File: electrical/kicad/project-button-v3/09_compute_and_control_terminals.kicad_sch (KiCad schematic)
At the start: 3 parts

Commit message: Add native DYNAMIXEL star injection release candidate
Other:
- title: PB HR-V0 Electrical V3 - 09 -> PB HR-V0 V3-P1.2 - 09
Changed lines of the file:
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@@
   (version 20250114) (generator "eeschema") (generator_version "10.0")
  (paper "A3")
-  (title_block (title "PB HR-V0 Electrical V3 - 09") (date "2026-08-06") (rev "V3-P1.1")
+  (title_block (title "PB HR-V0 V3-P1.2 - 09") (date "2026-08-07") (rev "V3-P1.2")
     (company "Project Button") (comment 1 "PRELIMINARY - NOT APPROVED FOR FABRICATION OR ENERGIZATION") (comment 2 "CONNECTED DESIGN CANDIDATE - QUALIFIED REVIEW REQUIRED"))
   (text "PRELIMINARY - NOT APPROVED FOR FABRICATION OR ENERGIZATION" (exclude_from_sim no) (at 17.78 10.16 0)

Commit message: Document HR-V0 contactor application evidence
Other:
- title: PB HR-V0 V3-P1.2 - 09 -> PB HR-V0 V3-P1.3 - 09
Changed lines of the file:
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@@
   (version 20250114) (generator "eeschema") (generator_version "10.0")
  (paper "A3")
-  (title_block (title "PB HR-V0 V3-P1.2 - 09") (date "2026-08-07") (rev "V3-P1.2")
+  (title_block (title "PB HR-V0 V3-P1.3 - 09") (date "2026-08-07") (rev "V3-P1.3")
     (company "Project Button") (comment 1 "PRELIMINARY - NOT APPROVED FOR FABRICATION OR ENERGIZATION") (comment 2 "CONNECTED DESIGN CANDIDATE - QUALIFIED REVIEW REQUIRED"))
   (text "PRELIMINARY - NOT APPROVED FOR FABRICATION OR ENERGIZATION" (exclude_from_sim no) (at 17.78 10.16 0)

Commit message: Add received-lot control for reset and arm terminals
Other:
- title: PB HR-V0 V3-P1.3 - 09 -> PB HR-V0 V3-P1.4 - 09
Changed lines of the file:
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@@
   (version 20250114) (generator "eeschema") (generator_version "10.0")
  (paper "A3")
-  (title_block (title "PB HR-V0 V3-P1.3 - 09") (date "2026-08-07") (rev "V3-P1.3")
+  (title_block (title "PB HR-V0 V3-P1.4 - 09") (date "2026-08-07") (rev "V3-P1.4")
     (company "Project Button") (comment 1 "PRELIMINARY - NOT APPROVED FOR FABRICATION OR ENERGIZATION") (comment 2 "CONNECTED DESIGN CANDIDATE - QUALIFIED REVIEW REQUIRED"))
   (text "PRELIMINARY - NOT APPROVED FOR FABRICATION OR ENERGIZATION" (exclude_from_sim no) (at 17.78 10.16 0)

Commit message: Reconcile H1 pilot light in electrical V3
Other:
- title: PB HR-V0 V3-P1.4 - 09 -> PB HR-V0 V3-P1.5 - 09
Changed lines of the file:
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@@
   (version 20250114) (generator "eeschema") (generator_version "10.0")
  (paper "A3")
-  (title_block (title "PB HR-V0 V3-P1.4 - 09") (date "2026-08-07") (rev "V3-P1.4")
+  (title_block (title "PB HR-V0 V3-P1.5 - 09") (date "2026-08-07") (rev "V3-P1.5")
     (company "Project Button") (comment 1 "PRELIMINARY - NOT APPROVED FOR FABRICATION OR ENERGIZATION") (comment 2 "CONNECTED DESIGN CANDIDATE - QUALIFIED REVIEW REQUIRED"))
   (text "PRELIMINARY - NOT APPROVED FOR FABRICATION OR ENERGIZATION" (exclude_from_sim no) (at 17.78 10.16 0)

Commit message: Correct control-panel protection fit
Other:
- title: PB HR-V0 V3-P1.5 - 09 -> PB HR-V0 V3-P1.6 - 09
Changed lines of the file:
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@@
   (version 20250114) (generator "eeschema") (generator_version "10.0")
  (paper "A3")
-  (title_block (title "PB HR-V0 V3-P1.5 - 09") (date "2026-08-07") (rev "V3-P1.5")
+  (title_block (title "PB HR-V0 V3-P1.6 - 09") (date "2026-08-07") (rev "V3-P1.6")
     (company "Project Button") (comment 1 "PRELIMINARY - NOT APPROVED FOR FABRICATION OR ENERGIZATION") (comment 2 "CONNECTED DESIGN CANDIDATE - QUALIFIED REVIEW REQUIRED"))
   (text "PRELIMINARY - NOT APPROVED FOR FABRICATION OR ENERGIZATION" (exclude_from_sim no) (at 17.78 10.16 0)

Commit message: Screen service disconnect and freeze fuse end cover
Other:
- title: PB HR-V0 V3-P1.6 - 09 -> PB HR-V0 V3-P1.7 - 09
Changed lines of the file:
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@@
   (version 20250114) (generator "eeschema") (generator_version "10.0")
  (paper "A3")
-  (title_block (title "PB HR-V0 V3-P1.6 - 09") (date "2026-08-07") (rev "V3-P1.6")
+  (title_block (title "PB HR-V0 V3-P1.7 - 09") (date "2026-08-07") (rev "V3-P1.7")
     (company "Project Button") (comment 1 "PRELIMINARY - NOT APPROVED FOR FABRICATION OR ENERGIZATION") (comment 2 "CONNECTED DESIGN CANDIDATE - QUALIFIED REVIEW REQUIRED"))
   (text "PRELIMINARY - NOT APPROVED FOR FABRICATION OR ENERGIZATION" (exclude_from_sim no) (at 17.78 10.16 0)

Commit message: Freeze SD1 candidate and synchronize R64
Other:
- title: PB HR-V0 V3-P1.7 - 09 -> PB HR-V0 V3-P1.8 - 09
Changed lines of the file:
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@@
   (version 20250114) (generator "eeschema") (generator_version "10.0")
  (paper "A3")
-  (title_block (title "PB HR-V0 V3-P1.7 - 09") (date "2026-08-07") (rev "V3-P1.7")
+  (title_block (title "PB HR-V0 V3-P1.8 - 09") (date "2026-08-07") (rev "V3-P1.8")
     (company "Project Button") (comment 1 "PRELIMINARY - NOT APPROVED FOR FABRICATION OR ENERGIZATION") (comment 2 "CONNECTED DESIGN CANDIDATE - QUALIFIED REVIEW REQUIRED"))
   (text "PRELIMINARY - NOT APPROVED FOR FABRICATION OR ENERGIZATION" (exclude_from_sim no) (at 17.78 10.16 0)

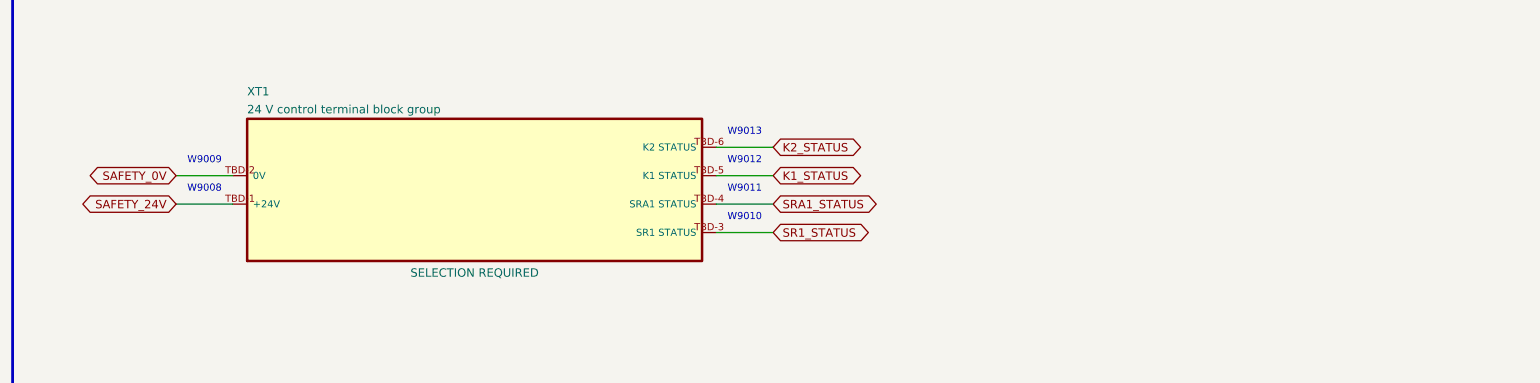
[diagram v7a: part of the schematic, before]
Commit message: Add R79 E2 hardware slice and Electrical V3-P1.9
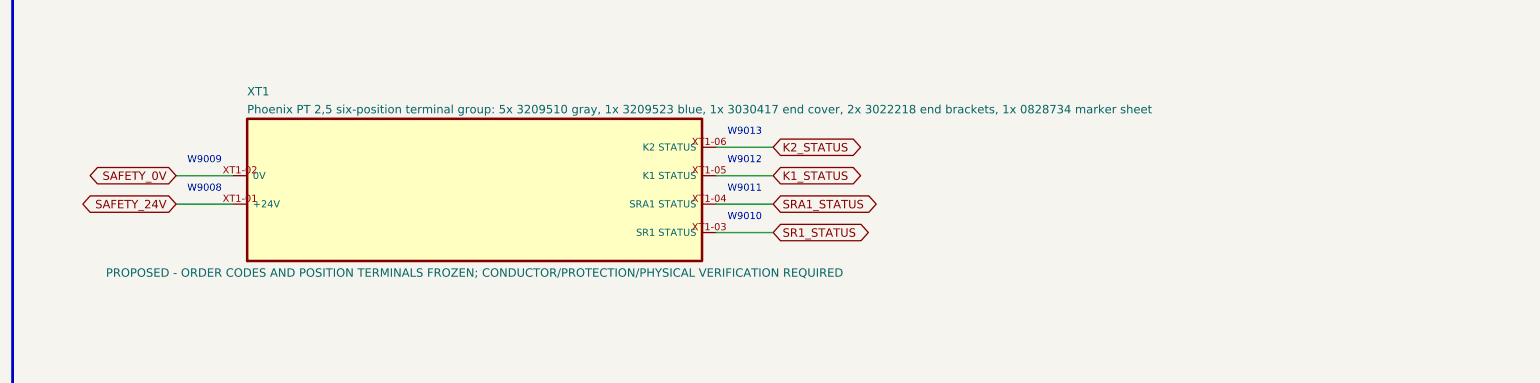
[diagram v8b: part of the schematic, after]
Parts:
- XT1: value 24 V control terminal block group -> Phoenix PT 2,5 six-position terminal group: 5x 3209510 gray, 1x 3209523 blue, 1x 3030417 end cover, 2x 3022218 end brac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; Display 24 V control terminal block group -> Phoenix PT 2,5 six-position terminal group: 5x 3209510 gray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; Evidence (none) -> Phoenix Contact current official product records for items 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; Status SELECTION REQUIRED -> PROPOSED - ORDER CODES AND POSITION TERMINALS FROZEN; CONDU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
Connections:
- net K1_STATUS: now also XT1.XT1-05 (K1 STATUS); no longer XT1.TBD-5 (K1 STATUS)
- net K2_STATUS: now also XT1.XT1-06 (K2 STATUS); no longer XT1.TBD-6 (K2 STATUS)
- net SAFETY_0V: now also XT1.XT1-02 (0V); no longer XT1.TBD-2 (0V)
- net SAFETY_24V: now also XT1.XT1-01 (+24V); no longer XT1.TBD-1 (+24V)
- net SR1_STATUS: now also XT1.XT1-03 (SR1 STATUS); no longer XT1.TBD-3 (SR1 STATUS)
- net SRA1_STATUS: now also XT1.XT1-04 (SRA1 STATUS); no longer XT1.TBD-4 (SRA1 STATUS)
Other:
- title: PB HR-V0 V3-P1.8 - 09 -> PB HR-V0 V3-P1.9 - 09
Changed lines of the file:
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@@
   (version 20250114) (generator "eeschema") (generator_version "10.0")
  (paper "A3")
-  (title_block (title "PB HR-V0 V3-P1.8 - 09") (date "2026-08-07") (rev "V3-P1.8")
+  (title_block (title "PB HR-V0 V3-P1.9 - 09") (date "2026-08-08") (rev "V3-P1.9")
     (company "Project Button") (comment 1 "PRELIMINARY - NOT APPROVED FOR FABRICATION OR ENERGIZATION") (comment 2 "CONNECTED DESIGN CANDIDATE - QUALIFIED REVIEW REQUIRED"))
   (text "PRELIMINARY - NOT APPROVED FOR FABRICATION OR ENERGIZATION" (exclude_from_sim no) (at 17.78 10.16 0)
@@
       (exclude_from_sim no) (in_bom yes) (on_board yes) (dnp no)
       (property "Reference" "XT1" (at 54.61 182.69 0) (effects (font (size 1.50 1.50)) (justify left bottom)))
-      (property "Value" "24 V control terminal block group" (at 95.25 199.39 0) (effects (font (size 1.50 1.50)) (hide yes)))
+      (property "Value" "Phoenix PT 2,5 six-position terminal group: 5x 3209510 gray, 1x 3209523 blue, 1x 3030417 end cover, 2x 3022218 end brackets, 1x 0828734 marker sheet" (at 95.25 199.39 0) (effects (font (size 1.50 1.50)) (hide yes)))
       (property "Footprint" "" (at 95.25 199.39 0) (effects (font (size 1.50 1.50)) (hide yes)))
-      (property "Datasheet" "" (at 95.25 199.39 0) (effects (font (size 1.50 1.50)) (hide yes)))
-      (property "Description" "Exact terminal family, end covers, jumpers, markers, conductor range and torque open." (at 95.25 199.39 0) (effects (font (size 1.50 1.50)) (hide yes)))
-      (property "Status" "SELECTION REQUIRED" (at 95.25 215.09 0) (effects (font (size 1.50 1.50)) (justify bottom)))
-      (property "Evidence" "" (at 95.25 199.39 0) (effects (font (size 1.50 1.50)) (hide yes)))
-      (property "Display" "24 V control terminal block group" (at 54.61 185.89 0) (effects (font (size 1.50 1.50)) (justify left bottom)))
-      (pin "TBD-1")
-      (pin "TBD-2")
-      (pin "TBD-3")
-      (pin "TBD-4")
-      (pin "TBD-5")
-      (pin "TBD-6")
+      (property "Datasheet" "https://www.phoenixcontact.com/en-us/products/feed-through-terminal-block-pt-25-3209510" (at 95.25 199.39 0) (effects (font (size 1.50 1.50)) (hide yes)))
+      (property "Description" "Exact six-position family and position-to-net allocation are frozen with no bridges. PT 2,5 item 3209510 and blue item 3209523 each provide two push-in connections and 5.2 mm width; D-ST 2,5 item 3030417 is the open-side end cover; two CLIPFIX 35 item 3022218 end brackets retain the group; UCT-TM 5 item 0828734 supplies 5.2 mm markers. Conductor order code, ferrule/direct-wire method, protection, current/temperature coordination, received compatibility, strip length, installed retention, marking and point-to-point evidence remain open." (at 95.25 199.39 0) (effects (font (size 1.50 1.50)) (hide yes)))
+      (property "Status" "PROPOSED - ORDER CODES AND POSITION TERMINALS FROZEN; CONDUCTOR/PROTECTION/PHYSICAL VERIFICATION REQUIRED" (at 95.25 215.09 0) (effects (font (size 1.50 1.50)) (justify bottom)))
+      (property "Evidence" "Phoenix Contact current official product records for items 3209510, 3209523, 3030417, 3022218 and 0828734; rechecked 2026-08-08." (at 95.25 199.39 0) (effects (font (size 1.50 1.50)) (hide yes)))
+      (property "Display" "Phoenix PT 2,5 six-position terminal group: 5x 3209510 gray, 1x 3209523 blue, 1x 3030417 end cover, 2x 3022218 end brackets, 1x 0828734 marker sheet" (at 54.61 185.89 0) (effects (font (size 1.50 1.50)) (justify left bottom)))
+      (pin "XT1-01")
+      (pin "XT1-02")
+      (pin "XT1-03")
+      (pin "XT1-04")
+      (pin "XT1-05")
+      (pin "XT1-06")
       (instances (project "project-button-v3" (path "/5cd52082-c883-51c8-b492-8b3b3e331e69/f3a60727-2e66-5730-a829-00cc7c809e89" (reference "XT1") (unit 1)))))
   (embedded_fonts no))
